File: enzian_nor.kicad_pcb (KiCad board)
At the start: 4 copper layers, 75 x 60 mm, 27 parts, among them IC1 L7809ABD2T-TR, J1 ASP-134488-01, U1 MT35XU02GCBA1G12-0AUT

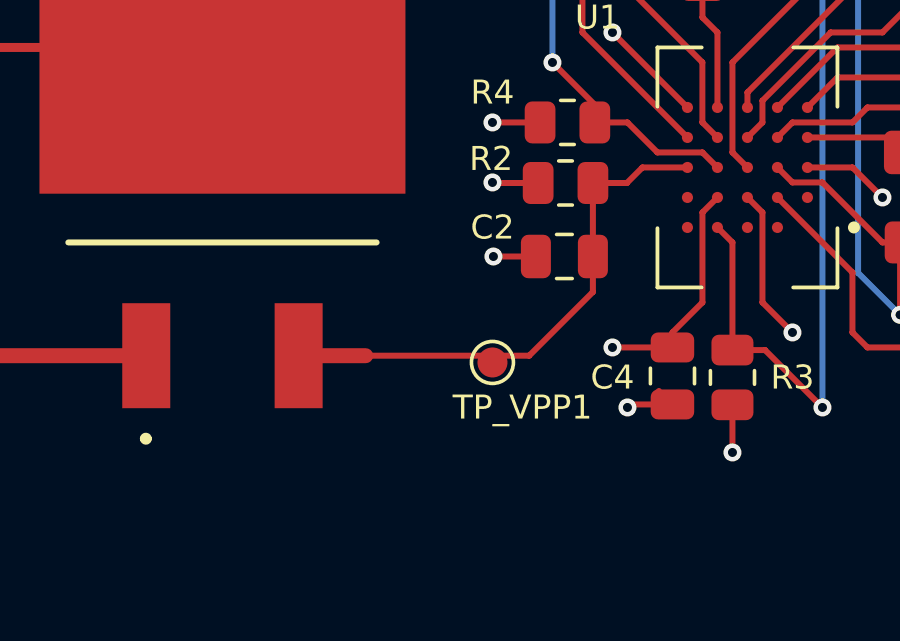
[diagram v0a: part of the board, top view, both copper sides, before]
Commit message: Place VPP capacitor closer to LDO
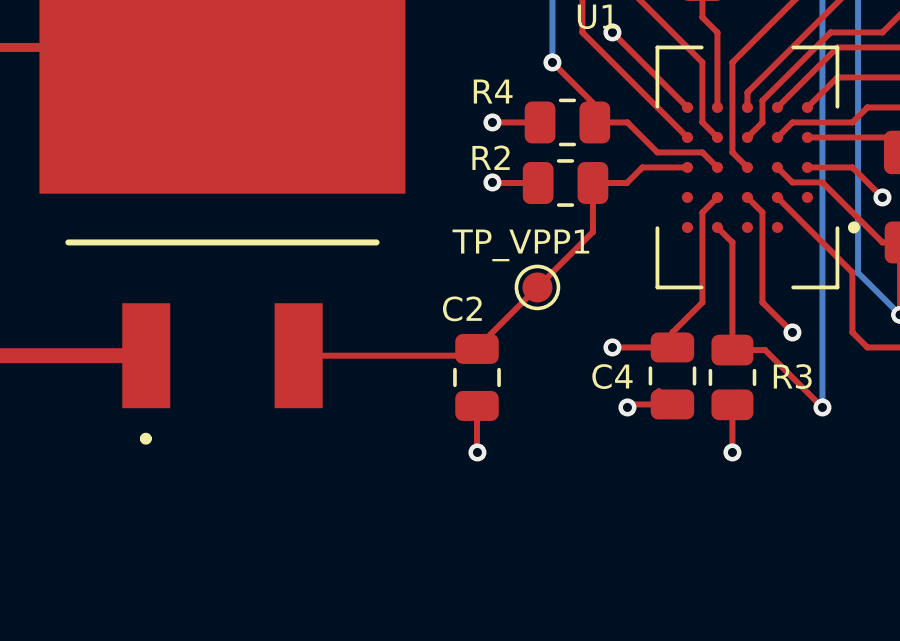
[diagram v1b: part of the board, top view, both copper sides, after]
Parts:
- moved C2 4.97 mm to (39.5, 116.0), turned to -90 degrees
- moved TP_VPP1 2.92 mm to (41.5, 113.0)
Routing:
- net /VPP: track 18.4 -> 16.7 mm
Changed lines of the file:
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@@
 	(footprint "Capacitor_SMD:C_0805_2012Metric"
 		(layer "F.Cu")
-		(at 42.398579 111.968324 180)
+		(at 39.484969 116 -90)
 		(descr "Capacitor SMD 0805 (2012 Metric), square (rectangular) end terminal, IPC-7351 nominal, (Body size source: IPC-SM-782 page 76, https://www.pcb-3d.com/wordpress/wp-content/uploads/ipc-sm-782a_amendment_1_and_2.pdf, https://docs.google.com/spreadsheets/d/1BsfQQcO9C6DZCsRaXUlFlo91Tg2WpOkGARC1WS5S8t0/edit?usp=sharing), generated with kicad-footprint-generator")
 		(tags "capacitor")
 		(property "Reference" "C2"
-			(at 2.398579 0.968324 0)
+			(at -2.256093 0.463659 180)
 			(layer "F.SilkS")
 			(effects
@@
 		)
 		(property "Value" "100n"
-			(at 0 1.68 0)
+			(at 0 1.68 90)
 			(layer "F.Fab")
 			(effects
@@
 		)
 		(property "Datasheet" "~"
-			(at 0 0 0)
+			(at 0 0 90)
 			(layer "F.Fab")
 			(hide yes)
@@
 		)
 		(property "Description" "Unpolarized capacitor, small symbol"
-			(at 0 0 0)
+			(at 0 0 90)
 			(layer "F.Fab")
 			(hide yes)
@@
 		)
 		(fp_line
-			(start 1.7 0.98)
-			(end -1.7 0.98)
+			(start -1.7 0.98)
+			(end -1.7 -0.98)
 			(stroke
 				(width 0.05)
@@
 		)
 		(fp_line
-			(start 1.7 -0.98)
-			(end 1.7 0.98)
+			(start 1.7 0.98)
+			(end -1.7 0.98)
 			(stroke
 				(width 0.05)
@@
 		)
 		(fp_line
-			(start -1.7 0.98)
-			(end -1.7 -0.98)
+			(start -1.7 -0.98)
+			(end 1.7 -0.98)
 			(stroke
 				(width 0.05)
@@
 		)
 		(fp_line
-			(start -1.7 -0.98)
-			(end 1.7 -0.98)
+			(start 1.7 -0.98)
+			(end 1.7 0.98)
 			(stroke
 				(width 0.05)
@@
 		)
 		(fp_line
-			(start 1 0.625)
-			(end -1 0.625)
+			(start -1 0.625)
+			(end -1 -0.625)
 			(stroke
 				(width 0.1)
@@
 		)
 		(fp_line
-			(start 1 -0.625)
-			(end 1 0.625)
+			(start 1 0.625)
+			(end -1 0.625)
 			(stroke
 				(width 0.1)
@@
 		)
 		(fp_line
-			(start -1 0.625)
-			(end -1 -0.625)
+			(start -1 -0.625)
+			(end 1 -0.625)
 			(stroke
 				(width 0.1)
@@
 		)
 		(fp_line
-			(start -1 -0.625)
-			(end 1 -0.625)
+			(start 1 -0.625)
+			(end 1 0.625)
 			(stroke
 				(width 0.1)
@@
 		)
 		(fp_text user "${REFERENCE}"
-			(at 0 0 0)
+			(at 0 0 90)
 			(layer "F.Fab")
 			(effects
@@
 		)
 		(pad "1" smd roundrect
-			(at -0.95 0 180)
+			(at -0.95 0 270)
 			(size 1 1.45)
 			(layers "F.Cu" "F.Mask" "F.Paste")
@@
 		)
 		(pad "2" smd roundrect
-			(at 0.95 0 180)
+			(at 0.95 0 270)
 			(size 1 1.45)
 			(layers "F.Cu" "F.Mask" "F.Paste")
@@
 	(footprint "TestPoint:TestPoint_Pad_D1.0mm"
 		(layer "F.Cu")
-		(at 40 115.5)
+		(at 41.5 113)
 		(descr "SMD pad as test Point, diameter 1.0mm")
 		(tags "test point SMD pad")
 		(property "Reference" "TP_VPP1"
-			(at 1 1.5 0)
+			(at -0.5 -1.5 0)
 			(layer "F.SilkS")
 			(effects
@@
 	)
 	(segment
-		(start 40 112)
-		(end 40.031676 111.968324)
-		(width 0.2)
-		(layer "F.Cu")
-		(net 406)
-	)
-	(segment
 		(start 49 110.5)
 		(end 48.5 110)
@@
 	)
 	(segment
-		(start 45.55 116.45)
-		(end 45.5 116.5)
+		(start 39.484969 118.484969)
+		(end 39.5 118.5)
 		(width 0.2)
 		(layer "F.Cu")
@@
 	)
 	(segment
-		(start 21.05 115.5)
-		(end 21.05 116.95)
-		(width 0.5)
+		(start 39.484969 116.95)
+		(end 39.484969 118.484969)
+		(width 0.2)
 		(layer "F.Cu")
 		(net 406)
 	)
 	(segment
-		(start 41.448579 111.968324)
-		(end 40.031676 111.968324)
+		(start 45.55 116.45)
+		(end 45.5 116.5)
 		(width 0.2)
 		(layer "F.Cu")
 		(net 406)
 	)
+	(segment
+		(start 21.05 115.5)
+		(end 21.05 116.95)
+		(width 0.5)
+		(layer "F.Cu")
+		(net 406)
+	)
 	(via
 		(at 57 108.5)
@@
 	)
 	(via
-		(at 40.031676 111.968324)
+		(at 39.5 118.5)
 		(size 0.6)
 		(drill 0.3)
@@
 	)
 	(segment
-		(start 33.54 115.275)
-		(end 35.775 115.275)
-		(width 0.5)
+		(start 39.259969 115.275)
+		(end 39.484969 115.05)
+		(width 0.2)
 		(layer "F.Cu")
 		(net 407)
@@
 	)
 	(segment
-		(start 43.348579 113.151421)
-		(end 43.348579 111.968324)
+		(start 33.54 115.275)
+		(end 39.259969 115.275)
 		(width 0.2)
 		(layer "F.Cu")
@@
 	)
 	(segment
-		(start 43.348579 109.518324)
-		(end 44.481676 109.518324)
+		(start 39.388188 115.275)
+		(end 39.484969 115.178219)
 		(width 0.2)
 		(layer "F.Cu")
@@
 	)
 	(segment
-		(start 44.481676 109.518324)
-		(end 45 109)
+		(start 39.484969 115.05)
+		(end 39.484969 115.015031)
 		(width 0.2)
 		(layer "F.Cu")
@@
 	)
 	(segment
-		(start 35.775 115.275)
-		(end 41.225 115.275)
+		(start 43.348579 109.518324)
+		(end 44.481676 109.518324)
 		(width 0.2)
 		(layer "F.Cu")
@@
 	)
 	(segment
-		(start 43.45 112.175)
-		(end 43.45 111.45)
+		(start 44.481676 109.518324)
+		(end 45 109)
 		(width 0.2)
 		(layer "F.Cu")
@@
 	)
 	(segment
-		(start 41.225 115.275)
-		(end 43.348579 113.151421)
+		(start 39.484969 115.015031)
+		(end 43.348579 111.151421)
 		(width 0.2)
 		(layer "F.Cu")
@@
 	)
 	(segment
-		(start 43.348579 111.968324)
+		(start 43.348579 111.151421)
 		(end 43.348579 109.518324)
 		(width 0.2)
